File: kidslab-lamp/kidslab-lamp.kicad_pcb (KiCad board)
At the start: 2 copper layers, 87.7 x 130.4 mm, 38 parts, among them U1 Pico

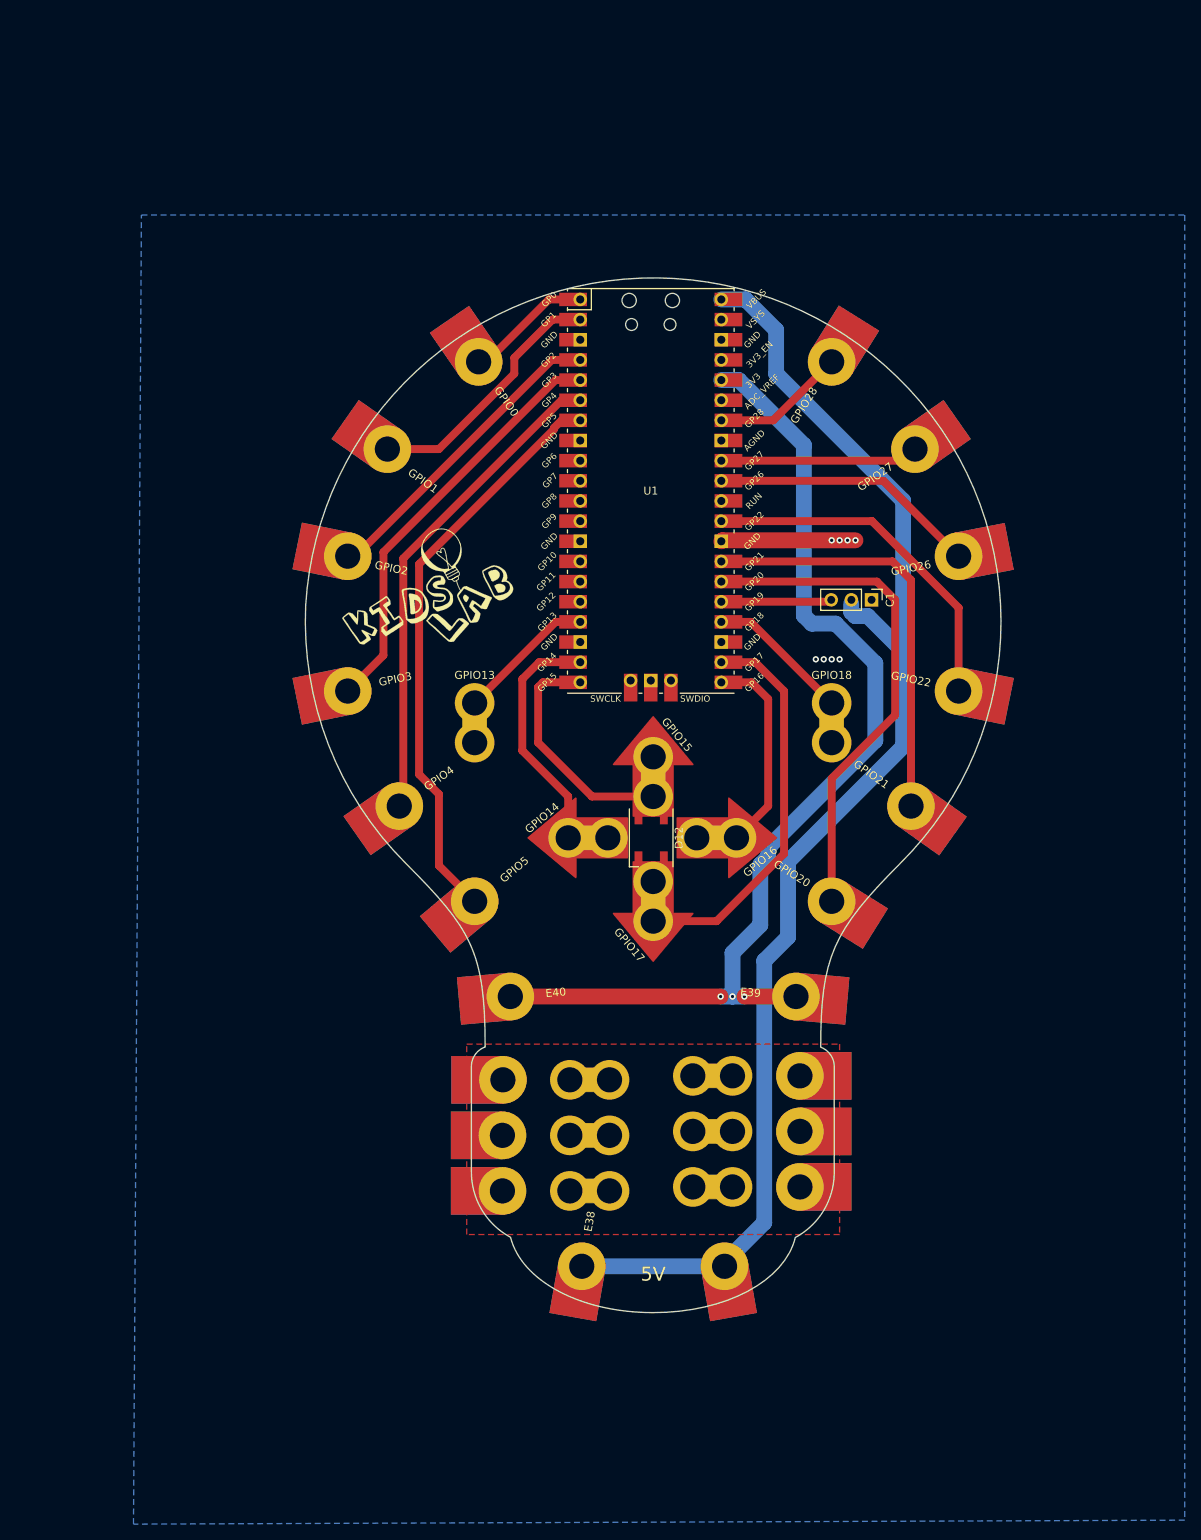
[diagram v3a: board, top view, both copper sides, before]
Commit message: finished design, further checks have to be done before ordering
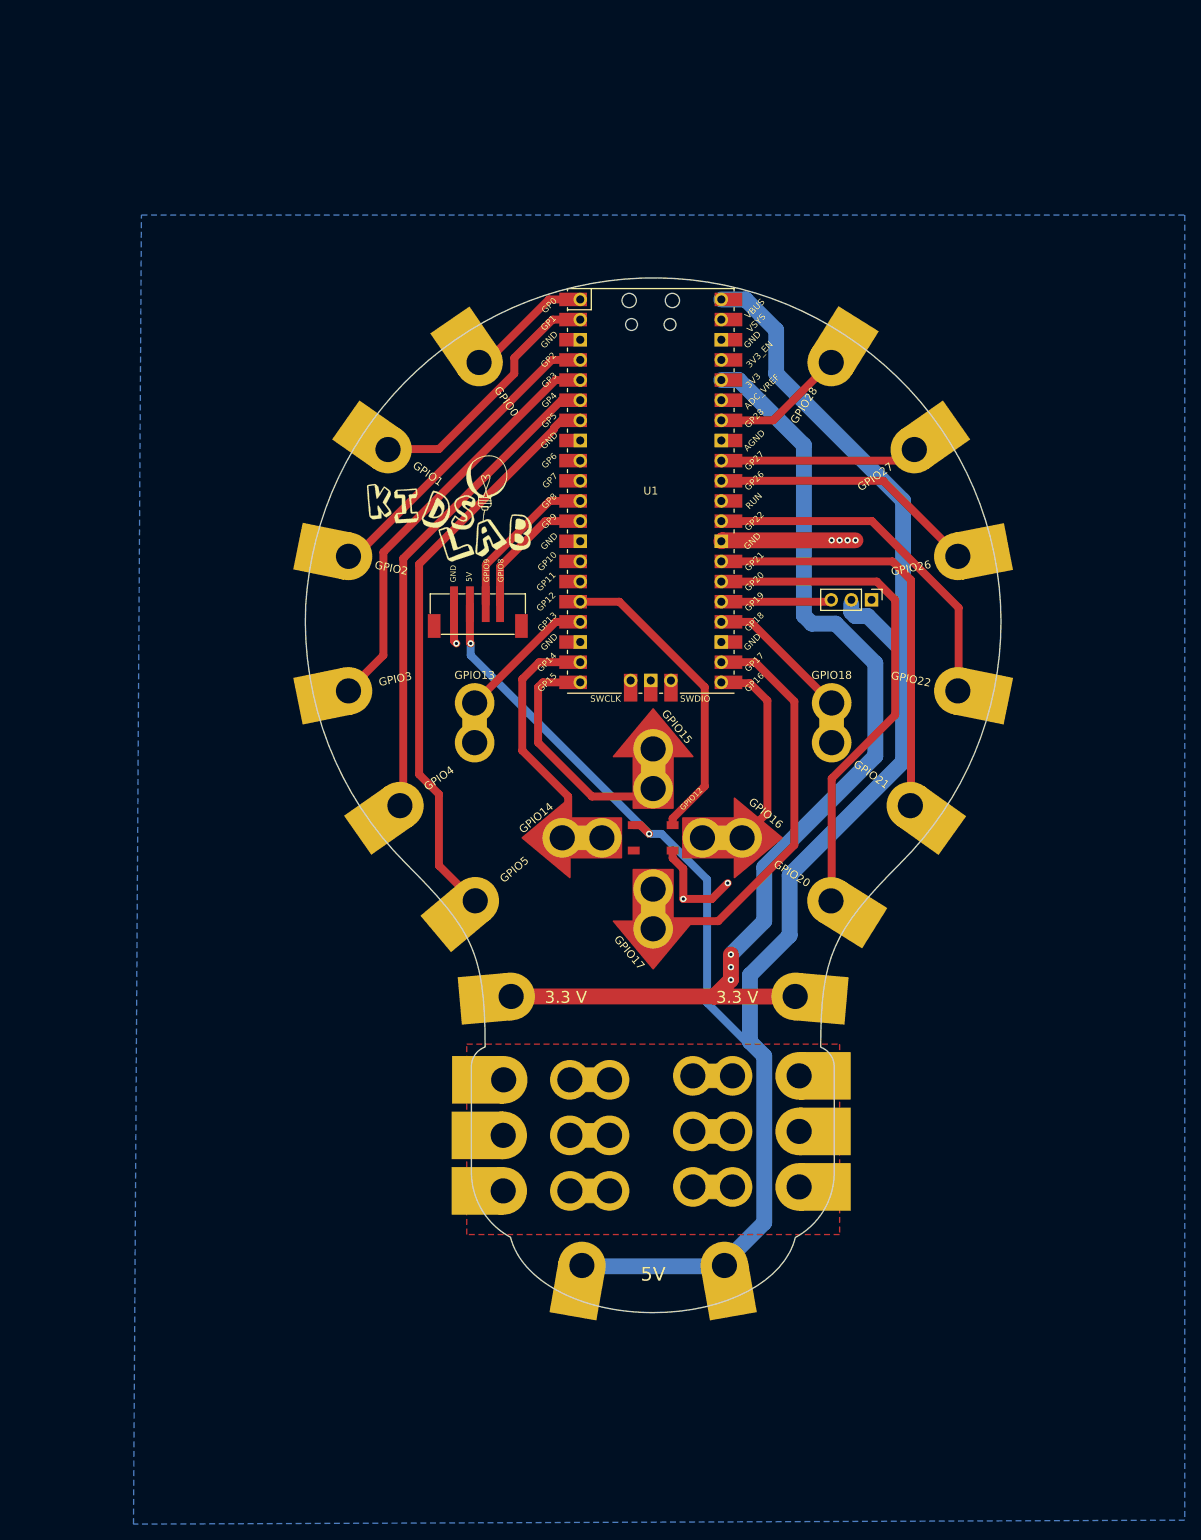
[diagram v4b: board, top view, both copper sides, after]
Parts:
- added C2: 114020163, kidslab:114020163, F.Cu at (127.8, 81.0)
- moved GPIO15 1.00 mm to (149.9, 100.4)
- moved GPIO17 0.96 mm to (149.9, 118.2)
- moved GPIO14 0.75 mm to (140.9, 109.2)
- moved GPIO16 0.71 mm to (158.7, 109.2)
- moved D12 0.25 mm to (149.9, 109.2), turned to 0 degrees
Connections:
- U1 pad 11: unconnected-(U1-Pad11) -> /grove_tx
- U1 pad 12: unconnected-(U1-Pad12) -> /grove_rx
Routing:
- net V_BUS: track 171.8 -> 249.2 mm, vias 0 -> 2
- net Net-(D12-Pad2): track 0.00 -> 39.2 mm
- net /grove_tx: track 0.00 -> 20.2 mm
- net GND: track 17.0 -> 35.1 mm, vias 8 -> 7
- net /grove_rx: track 0.00 -> 17.2 mm
- net Net-(GPIO17-Pad1): track 49.9 -> 51.1 mm
- net Net-(GPIO16-Pad1): track 25.9 -> 25.4 mm
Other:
- board text added: "3.3 V"
- board text added: "GND"
- board text added: "GPIO12"
- board text added: "GPIO8"
- board text added: "GPIO9"

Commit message: updated PCB with requested changes
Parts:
- removed GPIO20, GPIO5: kroko_edge, kidslab:Edgeconnector
- added C3: pin_header_1x3, Connector_PinHeader_2.54mm:PinHeader_1x03_P2.54mm_Vertical, F.Cu at (127.1, 72.4)
- added QR*****: https://tinyurl.com/ymjvzjzb, kidslab:kidslab-github, F.Cu at (175.3, 75.4)
- added R1: 10M, Resistor_THT:R_Axial_DIN0204_L3.6mm_D1.6mm_P5.08mm_Horizontal, F.Cu at (138.2, 116.8)
- added R2: 10M, Resistor_THT:R_Axial_DIN0204_L3.6mm_D1.6mm_P5.08mm_Horizontal, F.Cu at (141.2, 96.5)
- added R3: 10M, Resistor_THT:R_Axial_DIN0204_L3.6mm_D1.6mm_P5.08mm_Horizontal, F.Cu at (161.0, 101.6)
- added R4: 10M, Resistor_THT:R_Axial_DIN0204_L3.6mm_D1.6mm_P5.08mm_Horizontal, F.Cu at (158.0, 120.9)
- moved C1 51.5 mm to (127.1, 68.3), turned to 90 degrees
- moved E40 13.1 mm to (127.4, 116.8), turned to -140 degrees
- moved E39 11.1 mm to (171.6, 118.7), turned to -32 degrees
- moved C2 0.26 mm to (127.6, 81.0)
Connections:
- C1 pad 3: Net-(C1-Pad3) -> Net-(U1-Pad14)
- D12 pad 3: V_BUS -> 3.3V
- U1 pad 14: unconnected-(U1-Pad14) -> Net-(U1-Pad14)
- U1 pad 15: unconnected-(U1-Pad15) -> Net-(U1-Pad15)
- U1 pad 25: Net-(C1-Pad3) -> unconnected-(U1-Pad25)
- U1 pad 26: Net-(GPIO20-Pad1) -> unconnected-(U1-Pad26)
- U1 pad 7: Net-(GPIO5-Pad1) -> unconnected-(U1-Pad7)
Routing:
- net Net-(GPIO5-Pad1): track 73.3 -> 0.00 mm
- net 3.3V: track 132.8 -> 204.7 mm, vias 3 -> 8
- net Net-(GPIO20-Pad1): track 64.2 -> 0.00 mm
- net V_BUS: track 249.2 -> 271.5 mm, vias 2 -> 3
- net Net-(C1-Pad3): track 14.0 -> 0.00 mm
- net GND: track 35.1 -> 22.7 mm
- net Net-(GPIO17-Pad1): track 51.1 -> 62.7 mm
- net Net-(U1-Pad14): track 0.00 -> 11.1 mm
- net Net-(U1-Pad15): track 0.00 -> 10.4 mm
- net Net-(U1-Pad20): track 29.9 -> 40.1 mm
- net Net-(GPIO14-Pad1): track 30.6 -> 39.9 mm
- net Net-(GPIO16-Pad1): track 25.4 -> 34.4 mm
- net Net-(U1-Pad16): track 39.2 -> 41.7 mm
- net Net-(GPIO4-Pad1): track 62.0 -> 63.3 mm
- net /grove_tx: track 20.2 -> 19.5 mm, vias 0 -> 1
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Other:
- board text added: "GPIO10"
- board text added: "GPIO11"
- board text added: "USB"
